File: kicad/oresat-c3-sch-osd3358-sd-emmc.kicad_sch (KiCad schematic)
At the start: 66 parts, among them J4 DM3BT-DSF-PEJS, U1 OSD3358-512M-BSM, U24 25AAXX, U8 TCAN330, U9 EMMC+RESET+5.1-COMPATIBLE-BA

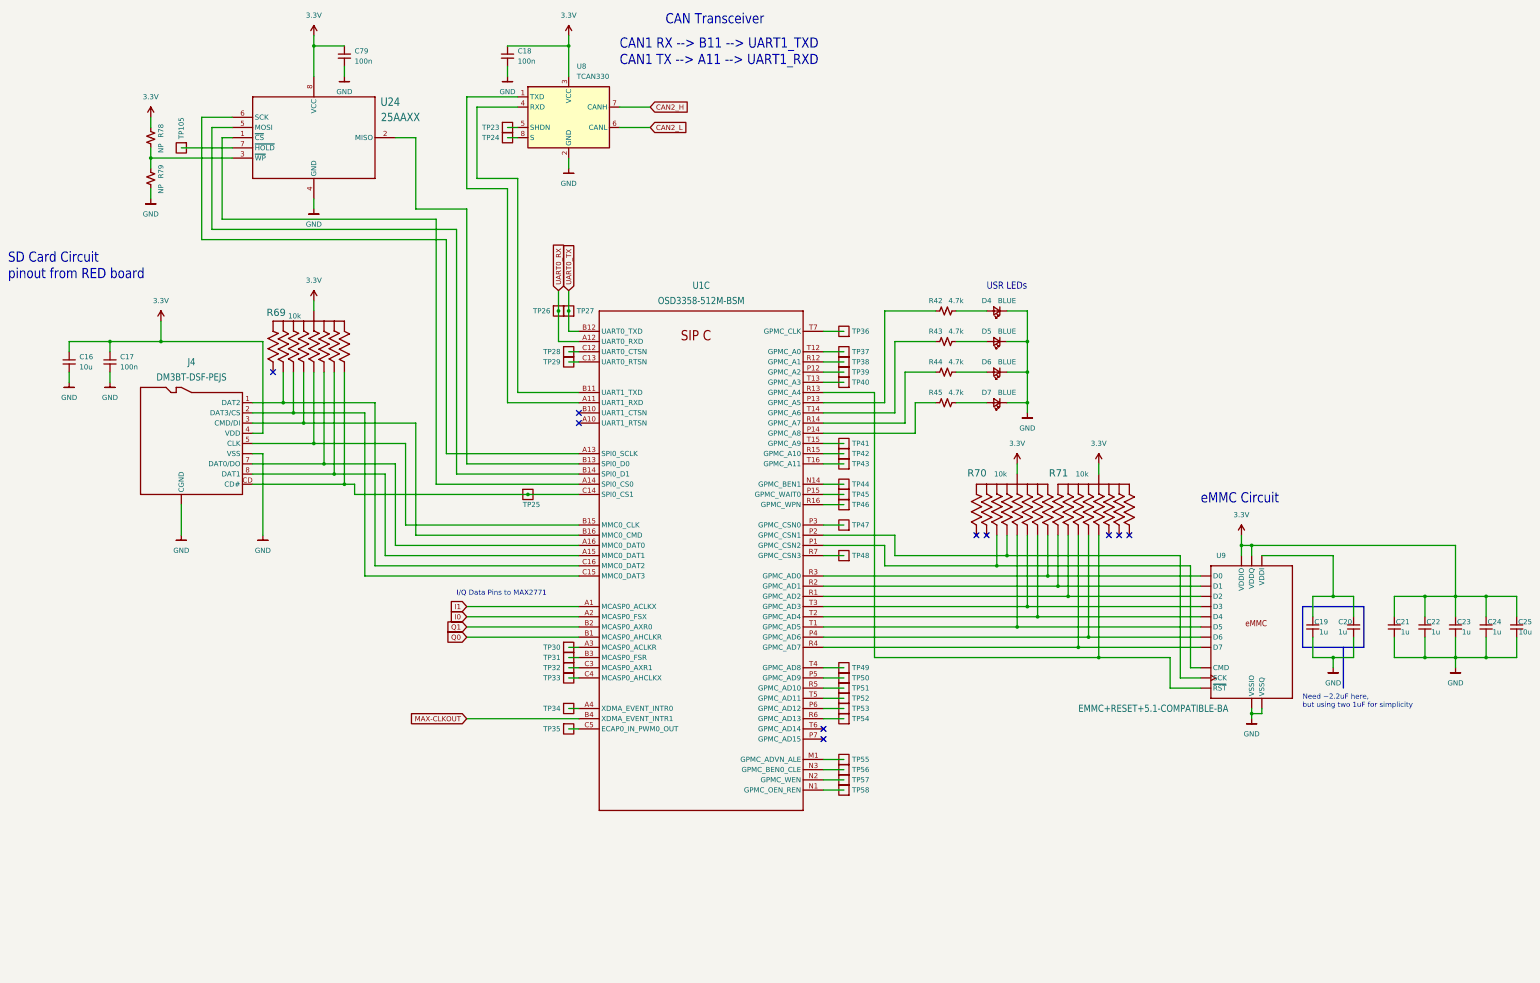
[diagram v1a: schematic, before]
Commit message: C3 v6 schematic now 80% done. OSD2258 IC has been gone over with a fine tooth comb and simplified as much as possible. OSD3358 pinout compared to RED board and PocketBeagle. What's left: lots of little issues, footprints, and then L band and UHF radio schematics need to be fixed.
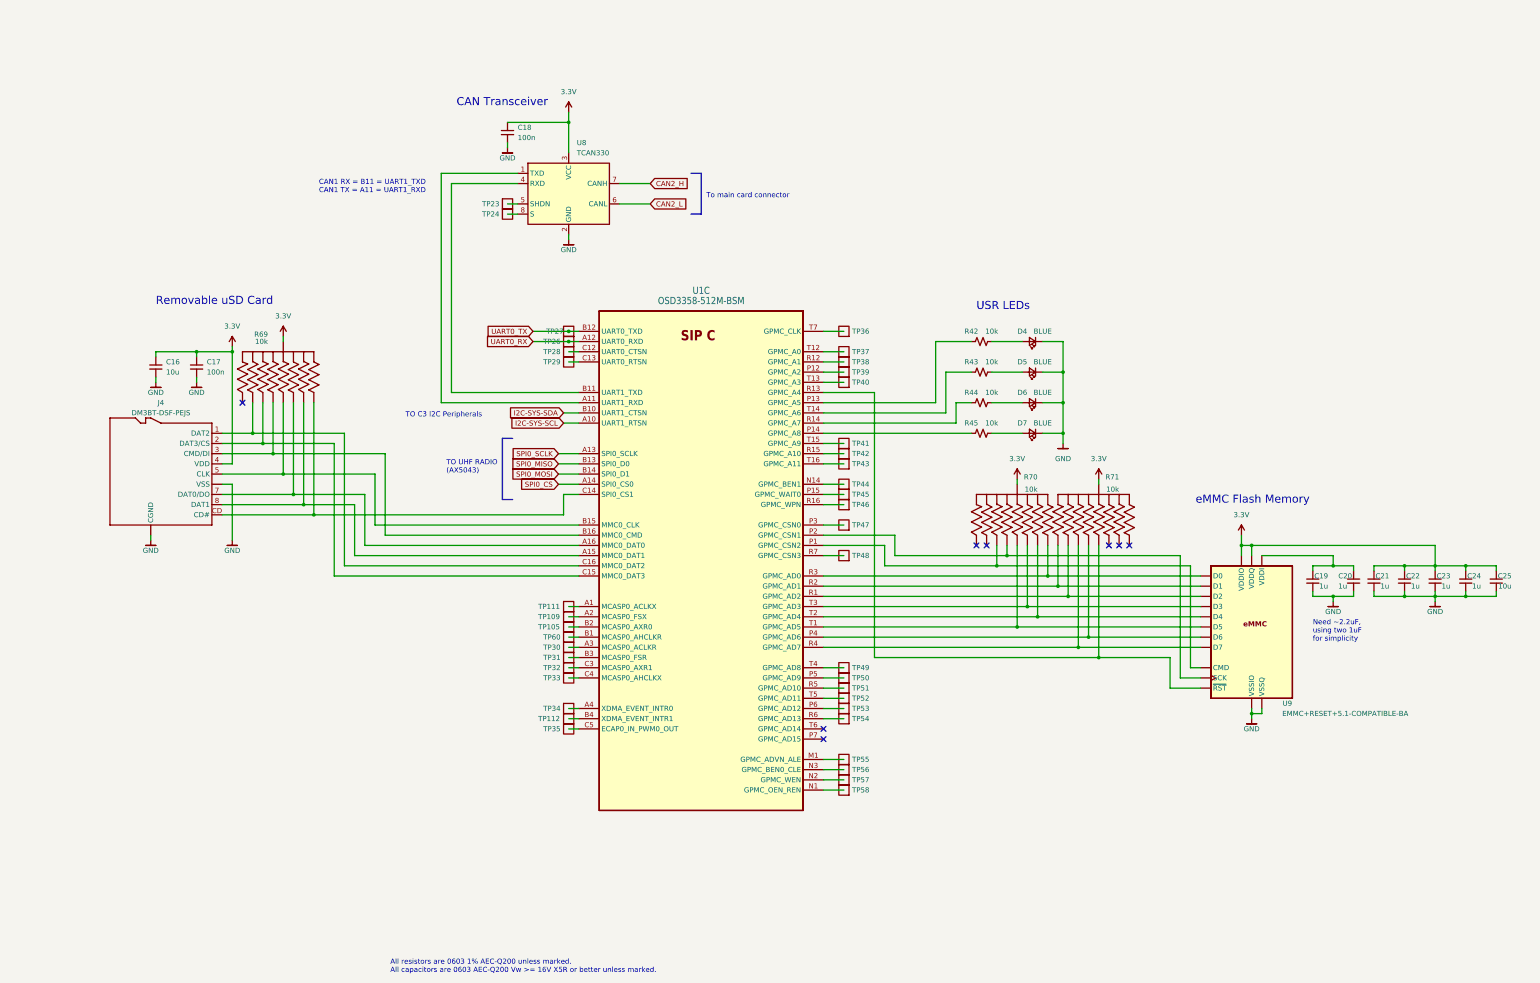
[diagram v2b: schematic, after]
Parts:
- removed C79: 100n, Capacitor_SMD:C_0603_1608Metric, symbol Device:C_Small
- removed R78, R79: NP, Resistor_SMD:R_0603_1608Metric, symbol Device:R_Small_US
- removed TP25: Test-Point, OreSat-TestPoint:PAD.03X.04, symbol OreSat-TestPoint:Test-Point
- removed U24: 25AAXX, Package_SO:SOIC-8_3.9x4.9mm_P1.27mm, symbol U-Microchip-25AAXXX-eeprom:25AAXX
- added TP109, TP111, TP112, TP60: Test-Point, OreSat-TestPoint:PAD.03X.04, symbol OreSat-TestPoint:Test-Point
- R42, R43, R44, R45: value 4.7k -> 10k
- U1: symbol U-OSD3358-512M-BSM:OSD3358-512M-BSM -> oresat-ics:OSD3358-512M-BSM
- U9: footprint oresat-footprints:BGA-153(11.5X13)(EMMC-BA) -> oresat-live-card:BGA-153(11.5X13)(EMMC-BA); symbol U-Generic-eMMC-153pin:EMMC+RESET+5.1-COMPATIBLE-BA -> oresat-ics:EMMC+RESET+5.1-COMPATIBLE-BA
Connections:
- net Q1 is gone; now on an unnamed net: U1.B2 (MCASP0_AXR0)
- net SPI0_CS: now reaches U1.A14 (SPI0_CS0)
- net SPI0_MISO: now reaches U1.B13 (SPI0_D0)
- net SPI0_MOSI: now reaches U1.B14 (SPI0_D1)
- net SPI0_SCLK: now reaches U1.A13 (SPI0_SCLK)
- net I2C-SYS-SCL: now reaches U1.A10 (UART1_RTSN)
- net I2C-SYS-SDA: now reaches U1.B10 (UART1_CTSN)
- net I0: no longer names the net of U1.A2 (MCASP0_FSX)
- net I0: now also TP109.1
- net I1: no longer names the net of U1.A1 (MCASP0_ACLKX)
- net I1: now also TP111.1
- net MAX-CLKOUT: no longer names the net of U1.B4 (XDMA_EVENT_INTR1)
- net MAX-CLKOUT: now also TP112.1
- net Q0: no longer names the net of U1.B1 (MCASP0_AHCLKR)
- net Q0: now also TP60.1
- no-connect marks 10 -> 8
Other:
- note added: "All resistors are 0603 1% AEC-Q200 unless marked. All capacitors are 0603 AEC-Q200 Vw >= 16V X5R or better unless marked."
- note added: "CAN1 RX = B11 = UART1_TXD CAN1 TX = A11 = UART1_RXD"
- note added: "Need ~2.2uF, using two 1uF for simplicity"
- note added: "Removable uSD Card"
- note added: "TO C3 I2C Peripherals"
- note added: "TO UHF RADIO (AX5043)"
- note added: "To main card connector"
- note added: "eMMC Flash Memory"
- note removed: "CAN1 RX --> B11 --> UART1_TXD CAN1 TX --> A11 --> UART1_RXD"
- note removed: "I/Q Data Pins to MAX2771"
- note removed: "Need ~2.2uF here, but using two 1uF for simplicity"
- note removed: "SD Card Circuit pinout from RED board"
- note removed: "eMMC Circuit"
- title: (none) -> OreSat C3: OSD3358 SIP C
- moved on the sheet: C16, C17, C18, C19, C20, C21, C22, C23, C24, C25, D4, D5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

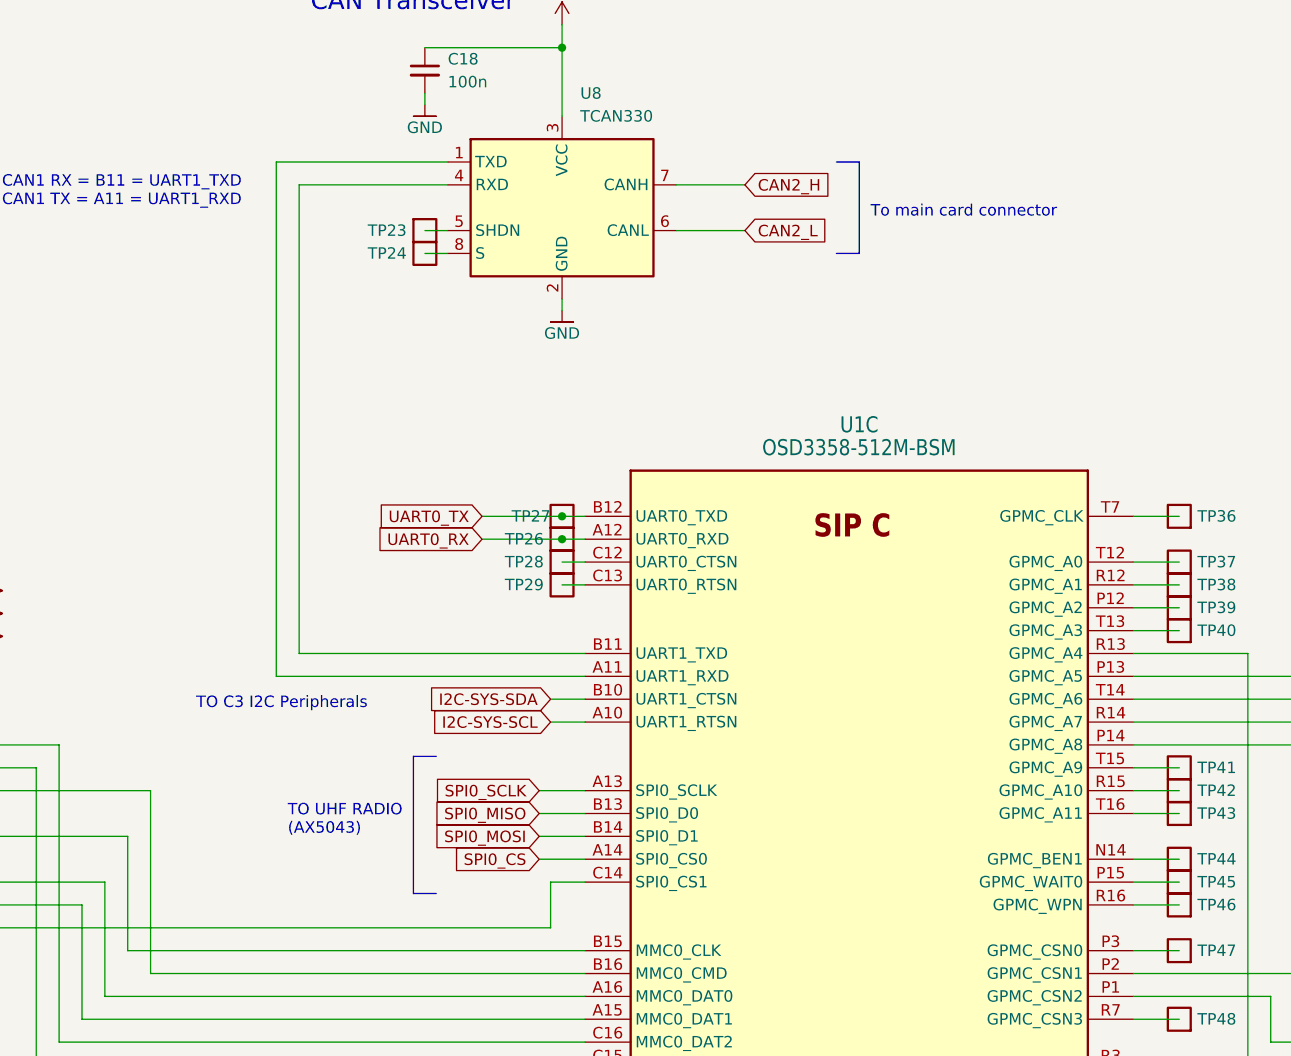
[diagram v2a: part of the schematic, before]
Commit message: Finished UHF radio schematic. Added sheet numbers to external labels. Still to do: L band radio, hooking up GPIO to the OSD3358, and test points.
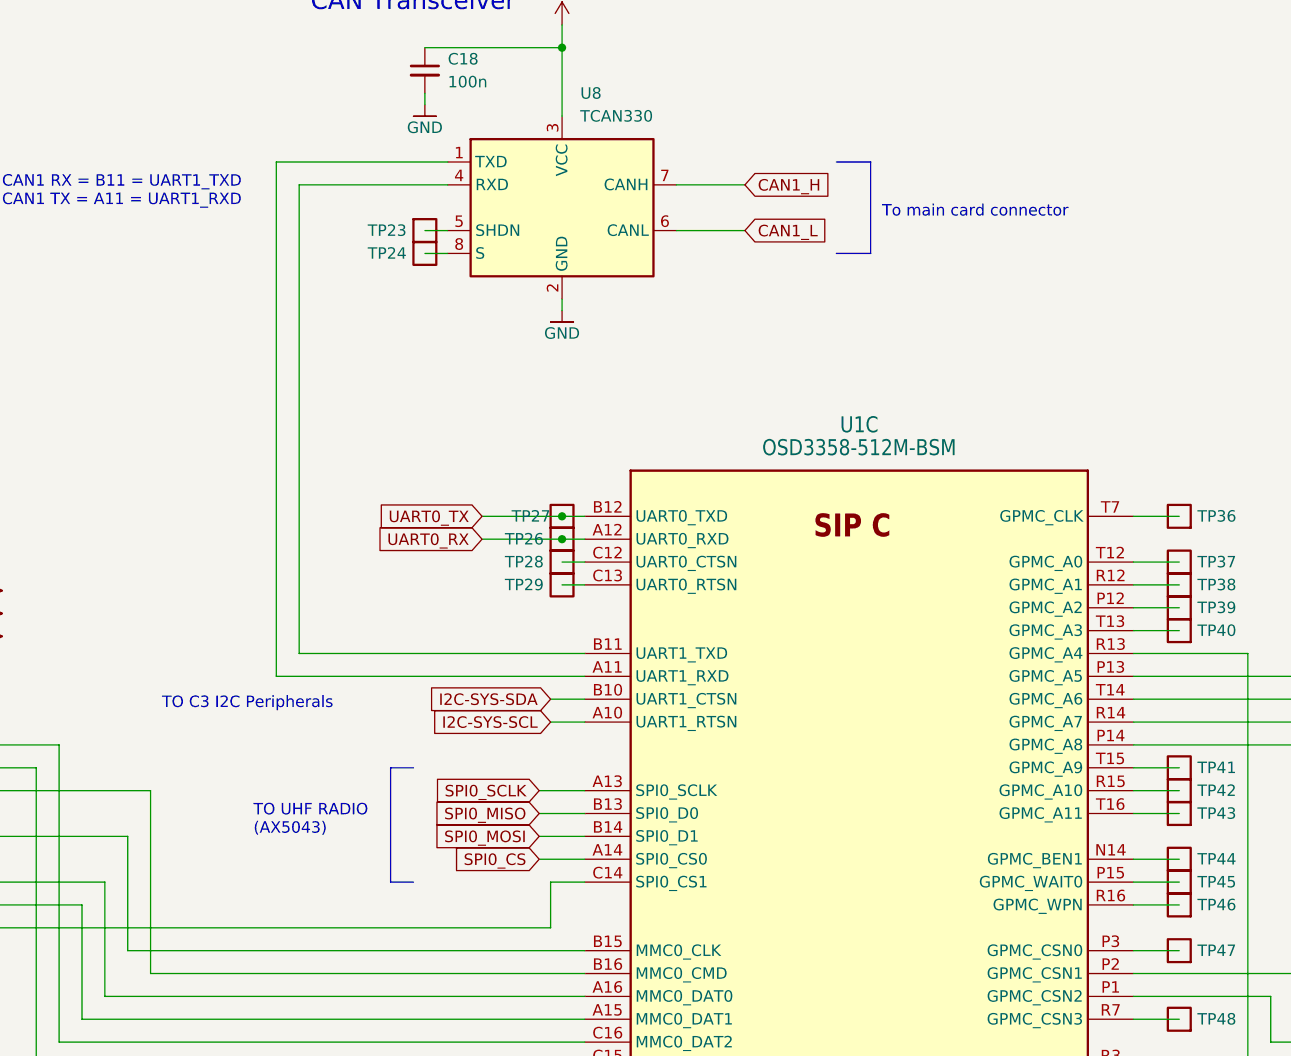
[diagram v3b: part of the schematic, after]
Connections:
- net CAN2_H renamed CAN1_H
- net CAN2_L renamed CAN1_L
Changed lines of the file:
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@@
     (stroke (width 0) (type default))
   )
-  (polyline (pts (xy 190.5 62.23) (xy 193.04 62.23))
+  (polyline (pts (xy 190.5 62.23) (xy 194.31 62.23))
     (stroke (width 0) (type default))
   )
@@
     (stroke (width 0) (type default))
   )
-  (polyline (pts (xy 146.05 128.27) (xy 143.51 128.27))
+  (polyline (pts (xy 143.51 129.54) (xy 140.97 129.54))
     (stroke (width 0) (type default))
   )
@@
     (stroke (width 0) (type default))
   )
-  (polyline (pts (xy 190.5 72.39) (xy 193.04 72.39))
+  (polyline (pts (xy 190.5 72.39) (xy 194.31 72.39))
     (stroke (width 0) (type default))
   )
@@
     (stroke (width 0) (type default))
   )
-  (polyline (pts (xy 143.51 143.51) (xy 146.05 143.51))
+  (polyline (pts (xy 140.97 142.24) (xy 143.51 142.24))
     (stroke (width 0) (type default))
   )
@@
     (stroke (width 0) (type default))
   )
-  (polyline (pts (xy 143.51 128.27) (xy 143.51 143.51))
+  (polyline (pts (xy 140.97 129.54) (xy 140.97 142.24))
     (stroke (width 0) (type default))
   )
@@
     (stroke (width 0) (type default))
   )
-  (polyline (pts (xy 193.04 62.23) (xy 193.04 72.39))
+  (polyline (pts (xy 194.31 62.23) (xy 194.31 72.39))
     (stroke (width 0) (type default))
   )
@@
     (effects (font (size 1.27 1.27)) (justify left bottom))
   )
-  (text "To main card connector" (at 194.31 68.58 0)
+  (text "To main card connector" (at 195.58 68.58 0)
     (effects (font (size 1.27 1.27)) (justify left bottom))
   )
@@
     (effects (font (size 2 2)) (justify left bottom))
   )
-  (text "TO C3 I2C Peripherals" (at 119.38 123.19 0)
+  (text "TO C3 I2C Peripherals" (at 115.57 123.19 0)
     (effects (font (size 1.27 1.27)) (justify left bottom))
   )
@@
     (effects (font (size 2 2)) (justify left bottom))
   )
-  (text "TO UHF RADIO\n(AX5043)" (at 129.54 137.16 0)
+  (text "TO UHF RADIO\n(AX5043)" (at 125.73 137.16 0)
     (effects (font (size 1.27 1.27)) (justify left bottom))
   )
@@
     (effects (font (size 1.27 1.27)) (justify right))
     (property "Intersheetrefs" "${INTERSHEET_REFS}" (at 144.7166 137.16 0)
-      (effects (font (size 1.27 1.27)) (justify right) hide)
+      (effects (font (size 1.27 1.27)) (justify right))
     )
   )
@@
     (effects (font (size 1.27 1.27)) (justify right))
     (property "Intersheetrefs" "${INTERSHEET_REFS}" (at 144.5352 132.08 0)
-      (effects (font (size 1.27 1.27)) (justify right) hide)
+      (effects (font (size 1.27 1.27)) (justify right))
     )
   )
@@
     (effects (font (size 1.27 1.27)) (justify right))
     (property "Intersheetrefs" "${INTERSHEET_REFS}" (at 144.7166 134.62 0)
-      (effects (font (size 1.27 1.27)) (justify right) hide)
+      (effects (font (size 1.27 1.27)) (justify right))
     )
   )
@@
     (effects (font (size 1.27 1.27)) (justify right))
     (property "Intersheetrefs" "${INTERSHEET_REFS}" (at 142.5394 121.92 0)
-      (effects (font (size 1.27 1.27)) (justify right) hide)
+      (effects (font (size 1.27 1.27)) (justify right))
     )
   )
@@
     (effects (font (size 1.27 1.27)) (justify right))
     (property "Intersheetrefs" "${INTERSHEET_REFS}" (at 142.5999 124.46 0)
-      (effects (font (size 1.27 1.27)) (justify right) hide)
+      (effects (font (size 1.27 1.27)) (justify right))
     )
   )
@@
     (effects (font (size 1.27 1.27)) (justify right))
     (property "Intersheetrefs" "${INTERSHEET_REFS}" (at 138.9109 104.14 0)
-      (effects (font (size 1.27 1.27)) (justify right) hide)
+      (effects (font (size 1.27 1.27)) (justify right))
     )
   )
@@
     (effects (font (size 1.27 1.27)) (justify right))
     (property "Intersheetrefs" "${INTERSHEET_REFS}" (at 146.8333 139.7 0)
-      (effects (font (size 1.27 1.27)) (justify right) hide)
-    )
-  )
-  (global_label "CAN2_L" (shape input) (at 180.34 69.85 0) (fields_autoplaced)
+      (effects (font (size 1.27 1.27)) (justify right))
+    )
+  )
+  (global_label "CAN1_L" (shape input) (at 180.34 69.85 0) (fields_autoplaced)
     (effects (font (size 1.27 1.27)) (justify left))
-    (property "Intersheetrefs" "${INTERSHEET_REFS}" (at 189.6474 69.7706 0)
-      (effects (font (size 1.27 1.27)) (justify left) hide)
-    )
-  )
-  (global_label "CAN2_H" (shape input) (at 180.34 64.77 0) (fields_autoplaced)
+    (property "Intersheetrefs" "${INTERSHEET_REFS}" (at 190.1401 69.85 0)
+      (effects (font (size 1.27 1.27)) (justify left))
+    )
+  )
+  (global_label "CAN1_H" (shape input) (at 180.34 64.77 0) (fields_autoplaced)
     (effects (font (size 1.27 1.27)) (justify left))
-    (property "Intersheetrefs" "${INTERSHEET_REFS}" (at 189.9498 64.6906 0)
-      (effects (font (size 1.27 1.27)) (justify left) hide)
+    (property "Intersheetrefs" "${INTERSHEET_REFS}" (at 190.4425 64.77 0)
+      (effects (font (size 1.27 1.27)) (justify left))
     )
   )
@@
     (effects (font (size 1.27 1.27)) (justify right))
     (property "Intersheetrefs" "${INTERSHEET_REFS}" (at 139.2133 101.6 0)
-      (effects (font (size 1.27 1.27)) (justify right) hide)
-    )
-  )
+      (effects (font (size 1.27 1.27)) (justify right))
+    )
+  )
